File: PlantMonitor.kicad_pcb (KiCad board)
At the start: 2 copper layers, 2 parts, among them IC1 RFX2401C, U1 nRF24L01P

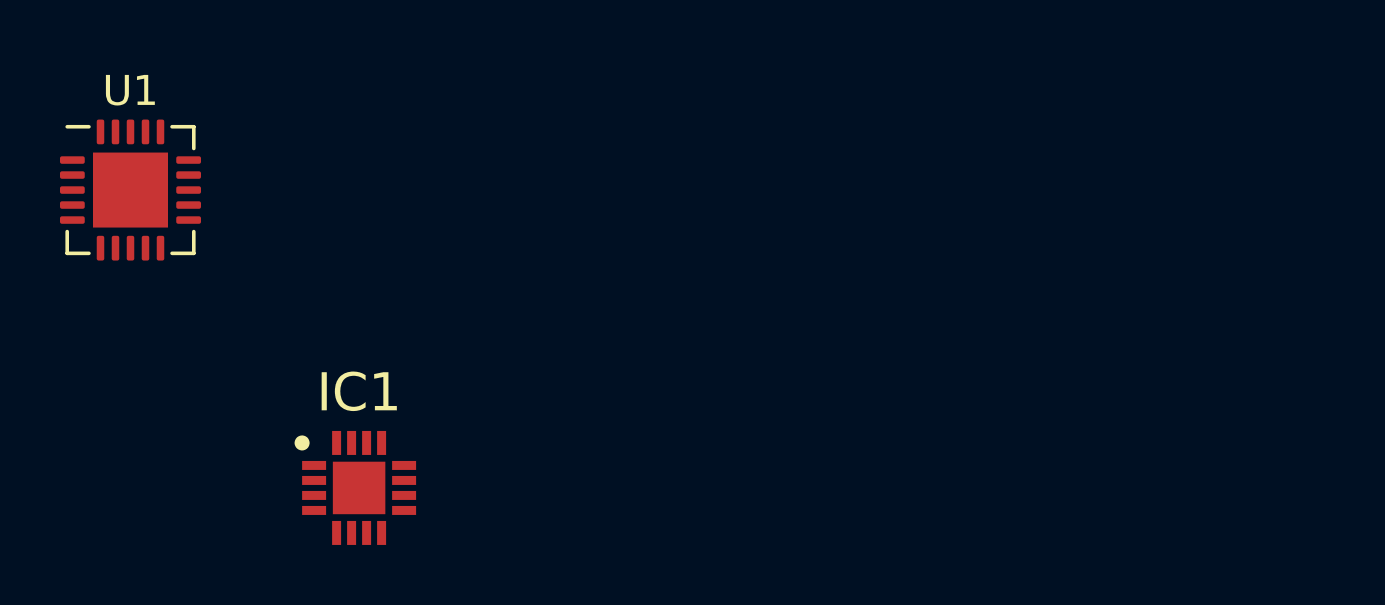
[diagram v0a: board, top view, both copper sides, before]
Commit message: First revision of RF circuit
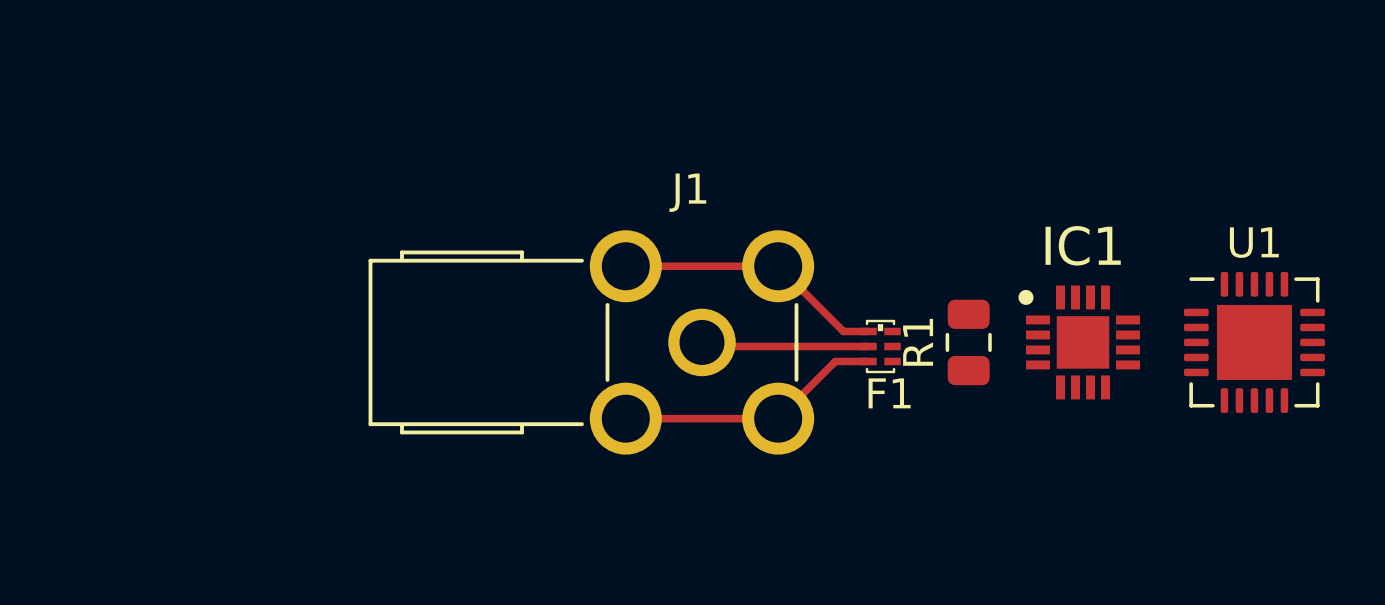
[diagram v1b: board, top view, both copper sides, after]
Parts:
- added F1: 2450LP14B100, Low pass filter:2450BM14A0002, F.Cu at (78.7, 66.7)
- added J1: 5-1814400-1, SMA Connector 5-1814400-1 TE Connectivity:SMA_CONN_5-1814400-1, F.Cu at (72.4, 66.0)
- added R1: R, Resistor_SMD:R_0805_2012Metric, F.Cu at (81.3, 66.0)
- moved U1 37.8 mm to (90.8, 66.0)
- moved IC1 24.6 mm to (85.1, 66.0)
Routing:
- net GND: track 0.00 -> 17.9 mm
- net Net-(F1-Pad5): track 0.00 -> 5.61 mm
